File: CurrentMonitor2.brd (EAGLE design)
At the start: 160 x 100 mm, 32 parts, among them IC1 MEGA8-AI, IC3 INA168, IC4 MAX3232CWE, J1 AVR_SPI_PRG_6OFFSET_PADS, Q1 10MHz, Q2 BSS123, U1 LCD-16X2NOSILK, X1 AKL701_213, X2 AKL701_213

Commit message: Added RS485 and WiFi options, finalized some parts of the design including order codes and prices @100pcs
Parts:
- removed IC4: MAX3232CWE, maxim:SO16L
- removed R7: 20k, rcl:RTRIM64W
- added C10, C11, C12, C13, C22: 100n, resistor:C0805
- added C14, C15: 22p, rcl:C0805
- added C16: 10µ, rcl:PANASONIC_B
- added C17: 22µ, rcl:PANASONIC_B
- added C19: 220µ, rcl:PANASONIC_D
- added C20, C24, C27, C31: 100n, rcl:C0805
- added C23: 100µ 63V, rcl:PANASONIC_G
- added C25: 220µ 10V, rcl:PANASONIC_D
- added D2: SK310A, diode:DO214AC
- added DC1: VA-0505S, dc-dc-converter:4SIL
- added IC12: 75176AD, 751xx:D_R-PDSO-G8
- added IC2: NCP1117ST33T3G, burr-brown:SOT223
- added IC5: MCP3426A0-E/SN, MCP3428:SOIC127P600X175-8N
- added JP11, JP12, JP13: (no value), jumper:JP1
- added L1: 2x51µH, epcos-b82790c0:EPCOS_B82790_SERIES
- added L2: 120µH, inductor-coilcraft:MSS1260
- added OK30, OK31, OK32: ACPL-M50L, ACPL-M50L:JEDEC_MS-012-AA_SOIC5
- added Q3: 10MHz, crystal:HC49UP
- added R11: 1k, rcl:R0805
- added R12: 120, rcl:R0805
- added R13, R14: 680, rcl:R0805
- added R34, R35, R36: 1k, resistor:R0805
- added R73, R74, R75: 220, resistor:R0805
- added U$2: LM2591HV, LM2591:TO263-5
- added U$3: (no value), Carambola2:CARAMBOLA2
- added U2: MAX232SOIC16, SparkFun:SO016
- added U3: FT232RL-BASICSSOP, SparkFun:SSOP28DB
- added U4: CD74HC4050M, SparkFun:SO016
- added U5: SC16IS740IPW,112, MCP3428:SOP65P640X110-16N
- added X4: SD-CONNECTOR104G-TAA0-R, con-sd-attend:104G-TAA0-R
- added X5: (no value), con-subd:F09HP
- C3, C4, C5, C6: value (none) -> 0.1µ
- C7, C8: device rcl:C1206 -> rcl:C0805
- IC1: value MEGA8-AI -> ATMEGA168A-AU
- R10: value 39k -> 33k
- R4: value 140k -> 110k
- X1, X2: value AKL701_213 -> 1714955
- moved X3 260.3 mm to (-156.2, -430.5)
- renumbered 0.003 to RS1
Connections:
- net N$10 renamed CONTRAST
- removed net N$15: C6.+, IC4.2
- removed net N$7: R10.2, R7.3
- removed net RXD: X3.2
- removed net TXD: X3.3
- new net CS: IC1.12, U4.3
- new net DMX_IN_A: L1.2
- new net DMX_IN_B: L1.4
- new net GNDI1: C19.-, C20.2, C24.2, C27.2, DC1.3, IC12.5, JP13.2, OK30.3, OK31.4, OK32.4
- new net N$10: D2.C, L2.P$2, U$2.2
- new net N$101: IC12.7, L1.3, R12.2, R14.2
- new net N$104: OK30.1, R75.1
- new net N$11: C3.-, U2.3
- new net N$116: OK31.1, R74.2
- new net N$133: OK32.1, R73.2
- new net N$17: C11.1, U3.17
- new net N$21: C14.2, Q3.2, U5.15
- new net N$22: C15.2, Q3.1, U5.16
- new net N$27: U4.2, X4.1
- new net N$28: U4.4, X4.2
- new net N$30: U4.6, X4.5
- new net N$53: IC12.6, JP11.1, L1.1, R13.1
- new net N$85: JP12.2, R13.2
- new net N$86: JP13.1, R14.1
- new net N$89: JP11.2, R12.1
- new net REC$1: IC12.1, R75.2
- new net RE_OUT: IC12.2, IC12.3, OK32.5, R34.1
- new net RTS: R73.1, U5.10
- new net RXD2_RS232: U2.8, X3.2
- new net RXD_RS485: OK30.5, R36.2, U5.13
- new net RXD_TTL_2: U$3.43, U2.9
- new net TXD2_RS232: U2.7, X3.3
- new net TXD_OUT: IC12.4, OK31.5, R35.1
- new net TXD_RS485: R74.1, U5.12
- new net TXD_TTL_2: U$3.44, U2.10
- new net UART_IRQ: IC1.32, R11.1, U5.7
- new net USB+: U$3.20, U3.15
- new net USB-: U$3.21, U3.16
- new net VCCIO1: C19.+, C20.1, C24.1, C27.1, DC1.4, IC12.8, JP12.1, OK31.6, OK32.6, R34.2, R35.2
- new net VIN: C23.+, U$2.1
- net +3V3: now also C13.2, C17.+, C22.1, IC2.2, R11.2, U$3.50, U$3.51, U4.1, U5.1, U5.14, U5.8, X4.4
- net +5V: now also C10.1, C12.2, C16.+, C25.+, C31.1, C6.-, DC1.2, IC2.3, IC5.3, L2.P$1, OK30.6, R36.1, U$2.4, U2.16, U3.20, U3.4; no longer IC4.16
- net ADC0: now also IC5.1; no longer IC1.23
- net ADC1: now also IC5.7, R10.2, R8.1; no longer IC1.24, R7.2
- net GND: now also C10.2, C11.2, C12.1, C13.1, C14.1, C15.1, C16.-, C17.-, C22.2, C31.2, DC1.1, IC2.1, IC5.2, IC5.6, IC5.8, OK30.4, OK31.3, OK32.3, U$3.22, U$3.25, U$3.27, U$3.28, U$3.29, U$3.30, U$3.31, U$3.32, U$3.34, U$3.42, U$3.45, U$3.46, U$3.47, U$3.48, U$3.49, U$3.7, U2.15, U3.18, U3.21, U3.25, U3.7, U4.8, U5.2, U5.3, U5.9, X3.G1, X3.G2, X4.3, X4.6, X4.GND1, X4.GND2, X4.GND3, X5.7, X5.G1, X5.G2; no longer C6.-, IC4.15
- net MISO: now also X4.7
- net MOSI: now also U4.5
- net N$12: now also C4.-, U2.5; no longer C4.+, IC4.4
- net N$13: now also C4.+, U2.4; no longer C4.-, IC4.5
- net N$14: now also C3.+, U2.1; no longer C5.-, IC4.6
- net N$6: now also C6.+, U2.2; no longer C3.-, IC4.3
- net N$8: now also C23.-, C25.-, D2.A, U$2.3, U$2.6; no longer R7.1, R8.1
- net N$9: now also C5.-, U2.6; no longer C3.+, IC4.1
- net RXD_RS232: now also U2.13, X5.2; no longer IC4.13
- net RXD_TTL: now also U2.12, U3.1; no longer IC4.12
- net SCK: now also U4.7
- net SCL: now also IC5.5, U5.5
- net SDA: now also IC5.4, U5.6
- net TXD_RS232: now also U2.14, X5.3; no longer IC4.14
- net TXD_TTL: now also U2.11, U3.5; no longer IC4.11

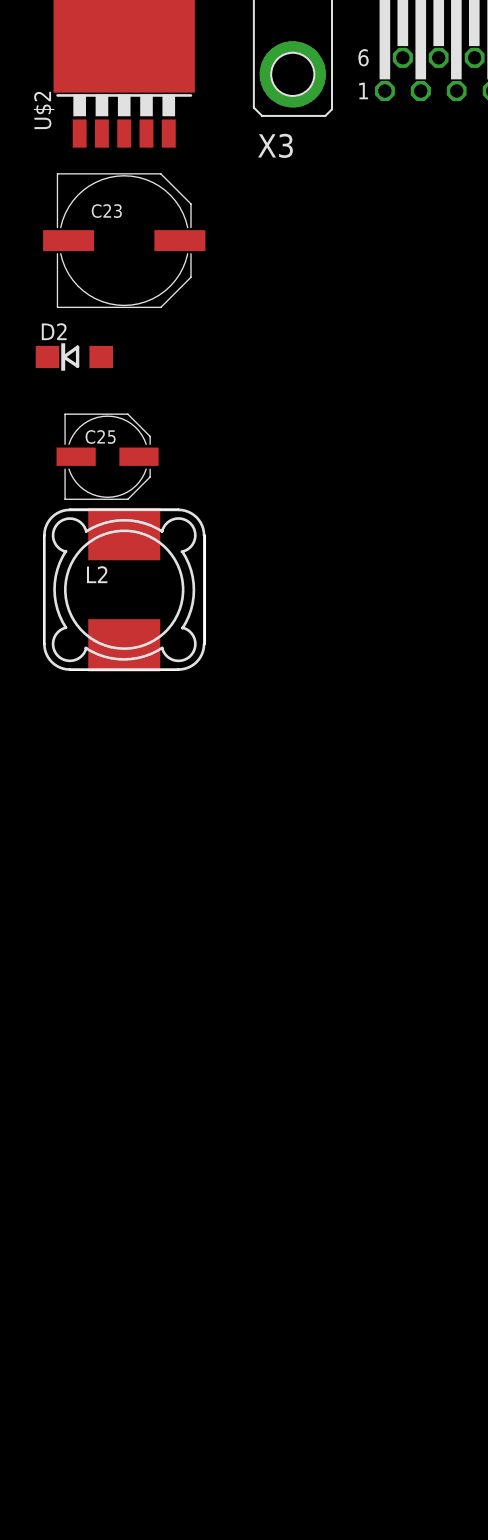
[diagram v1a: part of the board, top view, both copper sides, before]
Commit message: Added dual input switching power supplies and power switching circuitry
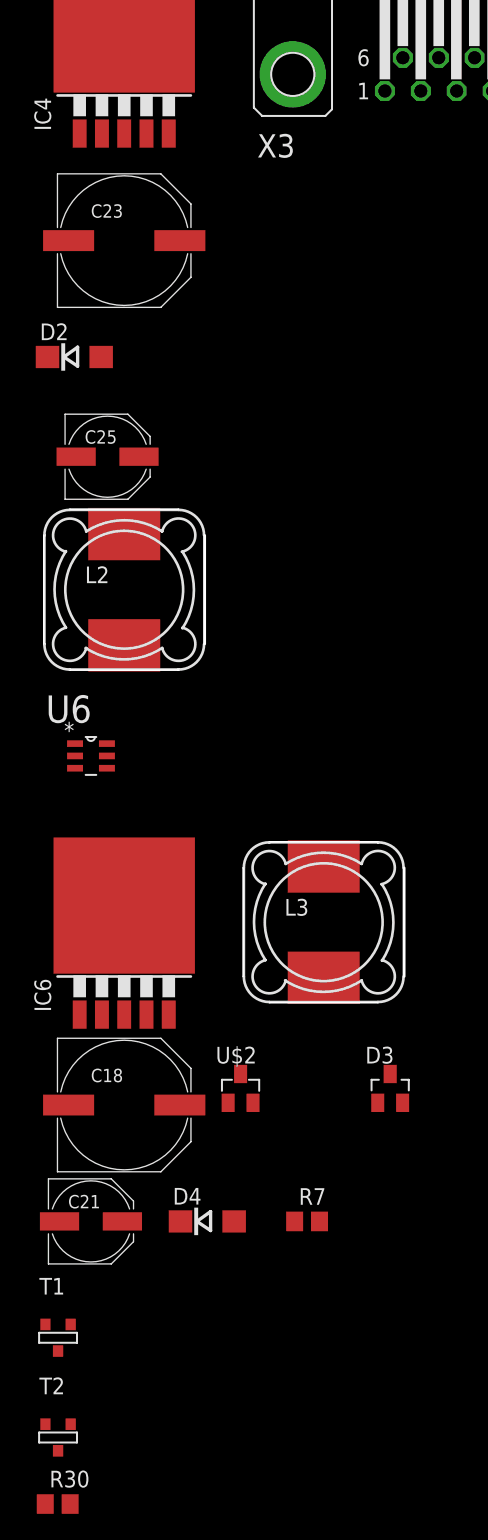
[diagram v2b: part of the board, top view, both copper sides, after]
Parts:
- added C18: 100µ 63V, rcl:PANASONIC_G
- added C21: 220µ 10V, rcl:PANASONIC_D
- added D3: 6V, diode:SOT23
- added D4: SK310A, diode:DO214AC
- added IC4, IC6: LM2591HV, LM2591:TO263-5
- added L3: 120µH, inductor-coilcraft:MSS1260
- added R30: 470k, rcl:R0805
- added R7: 100k, rcl:R0805
- added T1, T2: FDN306P, zetex:SOT-23
- added U6: LTC4412IS6TRMPBF, LTC4412:SOT95P280X100-6N
- D1: value 10V -> 6V
- U$2: value LM2591HV -> SI2309CDS; device LM2591:TO263-5 -> Si2309CDS:SOT23
- moved U$2 79.2 mm to (-172.7, -508.0)
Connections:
- removed net VOUT: D1.3, U$1.2
- new net +5V_1: C25.+, IC4.4, L2.P$1, T2.1, U6.1
- new net +5V_2: C21.+, IC6.4, L3.P$1, T1.1
- new net N$15: T2.3, U6.5
- new net N$7: D4.C, IC6.2, L3.P$2
- new net VIN1: C18.+, D3.3, IC6.1, U$2.2
- new net VIN_EXT: U$2.3
- net +5V: now also R30.2, T1.2, T2.2, U6.6; no longer C25.+, L2.P$1, U$2.4
- net GND: now also C18.-, C21.-, C23.-, C25.-, D2.A, D4.A, IC4.3, IC4.6, IC6.3, IC6.6, R7.1, U6.2, U6.3
- net N$10: now also IC4.2; no longer U$2.2
- net N$3: now also D3.1, R7.2, U$2.1; no longer U$1.3
- net N$8: now also R30.1, T1.3, U6.4; no longer C23.-, C25.-, D2.A, U$2.3, U$2.6
- net VIN: now also D1.3, IC4.1, U$1.2; no longer U$2.1
- net VIN_MEAS: now also U$1.3
